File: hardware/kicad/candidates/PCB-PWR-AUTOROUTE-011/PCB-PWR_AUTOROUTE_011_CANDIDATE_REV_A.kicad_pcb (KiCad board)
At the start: 4 copper layers, 90 x 60 mm, 66 parts, among them J1 43045-0213, J2 43045-1202, Q1 CSD18540Q5B, U1 LM74700QDBVRQ1, U2 INA226AIDGSR, U3 LMR604403SRAKR, U4 LMR604403SRAKR, U5 TPS7A2018PDBVR

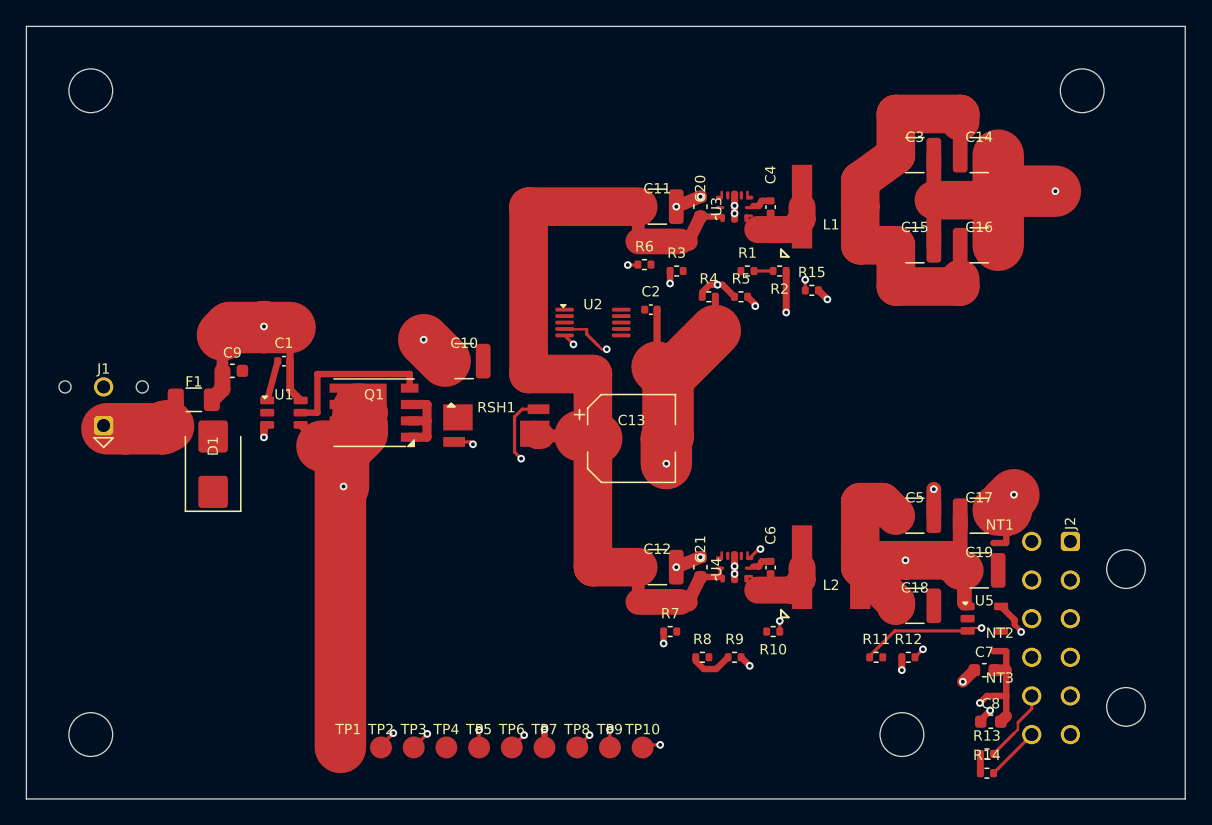
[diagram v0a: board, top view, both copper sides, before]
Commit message: apply: tools/apply_pcb_pwr_autoroute_candidate_rev_a.py
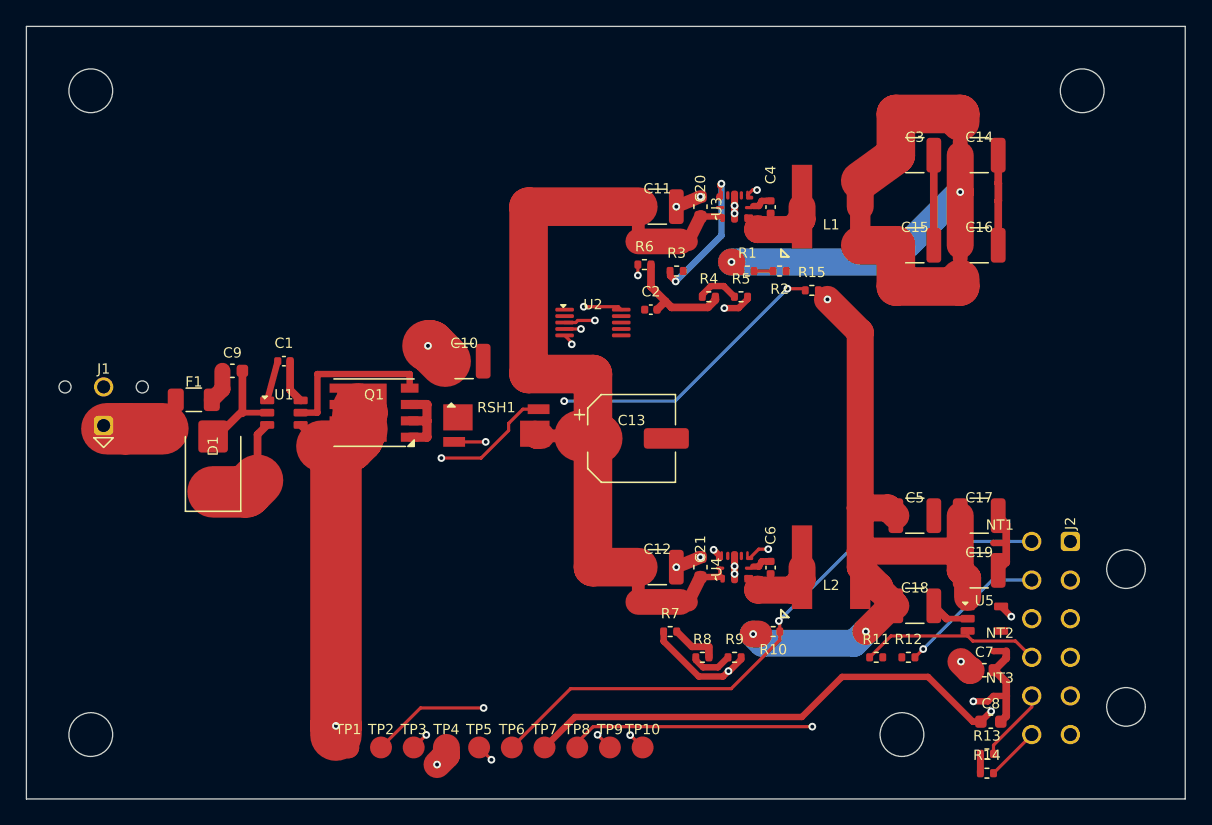
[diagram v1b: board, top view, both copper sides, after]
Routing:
- net 3V8_MODEM: track 34.0 -> 146.4 mm, vias 0 -> 3
- net FAULT: track 41.6 -> 82.8 mm, vias 2 -> 3
- net I2C2_SCL: track 73.4 -> 39.2 mm
- net I2C2_SDA: track 72.7 -> 40.0 mm
- net 3V3_DIGITAL: track 71.1 -> 93.9 mm
- net SHUNT_SOURCE_SENSE: track 28.0 -> 49.1 mm, vias 2 -> 3
- net VBAT_PROTECTED: track 53.5 -> 68.1 mm
- net EN_MODEM: track 50.4 -> 63.7 mm
- net VBAT_FUSED: track 33.2 -> 21.0 mm, vias 2 -> 0
- net GND_PWR: track 64.7 -> 53.3 mm, vias 13 -> 8
- net RT_3V3: track 9.28 -> 19.5 mm
- net RT_3V8: track 9.29 -> 18.3 mm, vias 2 -> 3
- net PG_3V8: track 55.8 -> 63.8 mm, vias 2 -> 4
- net 1V8_MIC: track 55.9 -> 52.9 mm, vias 3 -> 2
- net VBAT_RAW: track 7.51 -> 4.70 mm
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
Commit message: apply: tools/apply_pcb_pwr_autoroute_candidate_rev_a.py
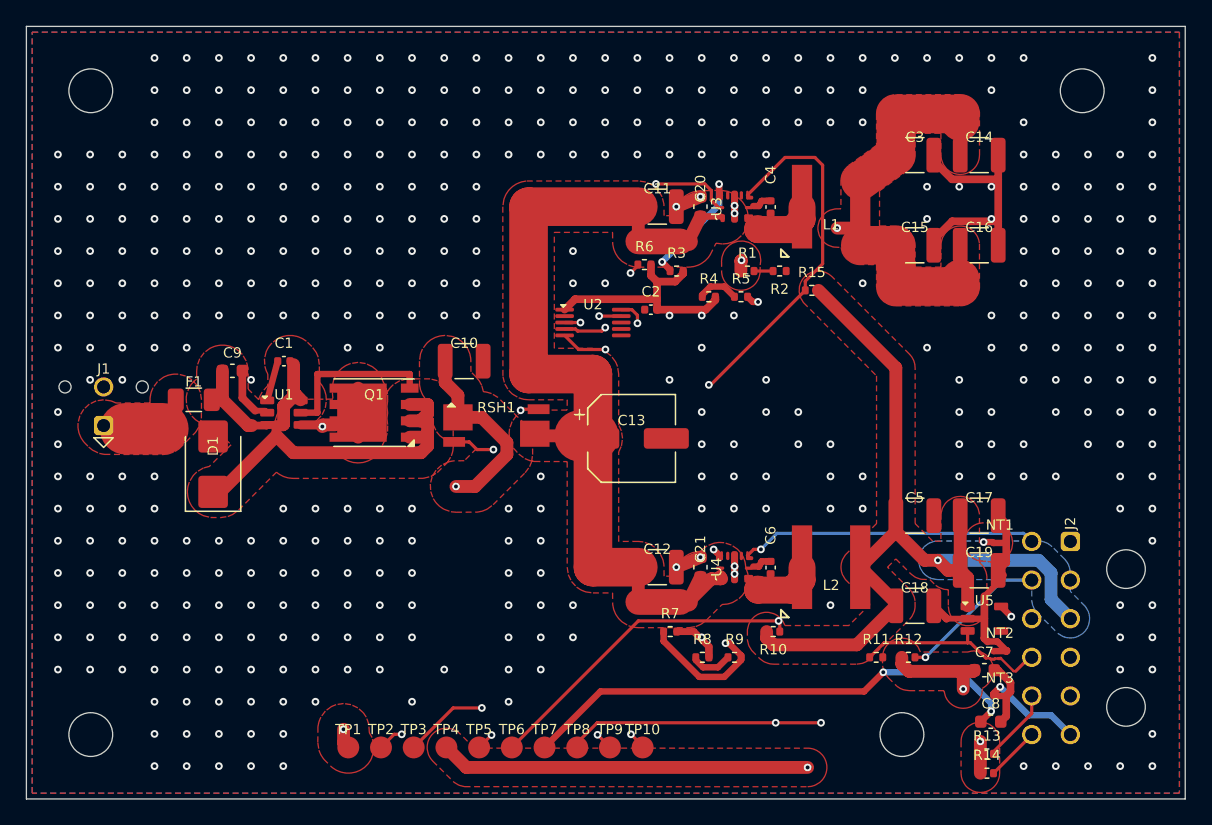
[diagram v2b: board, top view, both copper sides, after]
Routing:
- net VBAT_FUSED: track 21.0 -> 42.5 mm
- net GND_PWR: track 53.3 -> 72.7 mm, vias 8 -> 409
- net 3V8_MODEM: track 146.4 -> 132.3 mm
- net SHUNT_LOAD_SENSE: track 32.8 -> 43.9 mm, vias 2 -> 3
- net GND_MODEM: track 0.00 -> 8.74 mm, vias 0 -> 1
- net EN_MODEM: track 63.7 -> 71.9 mm, vias 1 -> 2
- net PG_3V8: track 63.8 -> 71.3 mm, vias 4 -> 2
- net VBAT_PROTECTED: track 68.1 -> 61.1 mm, vias 2 -> 3
- net I2C2_SDA: track 40.0 -> 45.3 mm
- net GND_MIC: track 11.7 -> 7.91 mm
- net 1V8_MIC: track 52.9 -> 55.7 mm, vias 2 -> 3
- net FAULT: track 82.8 -> 85.5 mm, vias 3 -> 4
- net VBAT_RAW: track 4.70 -> 7.37 mm
- net I2C2_SCL: track 39.2 -> 40.9 mm
- net SHUNT_SOURCE_SENSE: track 49.1 -> 50.7 mm
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- added copper zone on B.Cu, net 3V3_DIGITAL
- added copper zone on F.Cu, net 3V3_DIGITAL
- added copper zone on In2.Cu, net 3V3_DIGITAL
- added copper zone on F.Cu, net 3V8_MODEM
- added copper zone on In2.Cu, net 3V8_MODEM
- added copper zone on F.Cu, net GND_MODEM
- added copper zone on In2.Cu, net GND_MODEM
- added copper zone on B.Cu, net GND_PWR
- added copper zone on F.Cu, net GND_PWR
- added copper zone on F.Cu, net VBAT_FUSED
- added copper zone on F.Cu, net VBAT_PROTECTED
- added copper zone on In2.Cu, net VBAT_PROTECTED
- added copper zone on F.Cu, net VBAT_RAW
- added copper zone on F.Cu, net VBAT_SYS

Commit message: apply: tools/apply_pcb_pwr_autoroute_candidate_rev_a.py
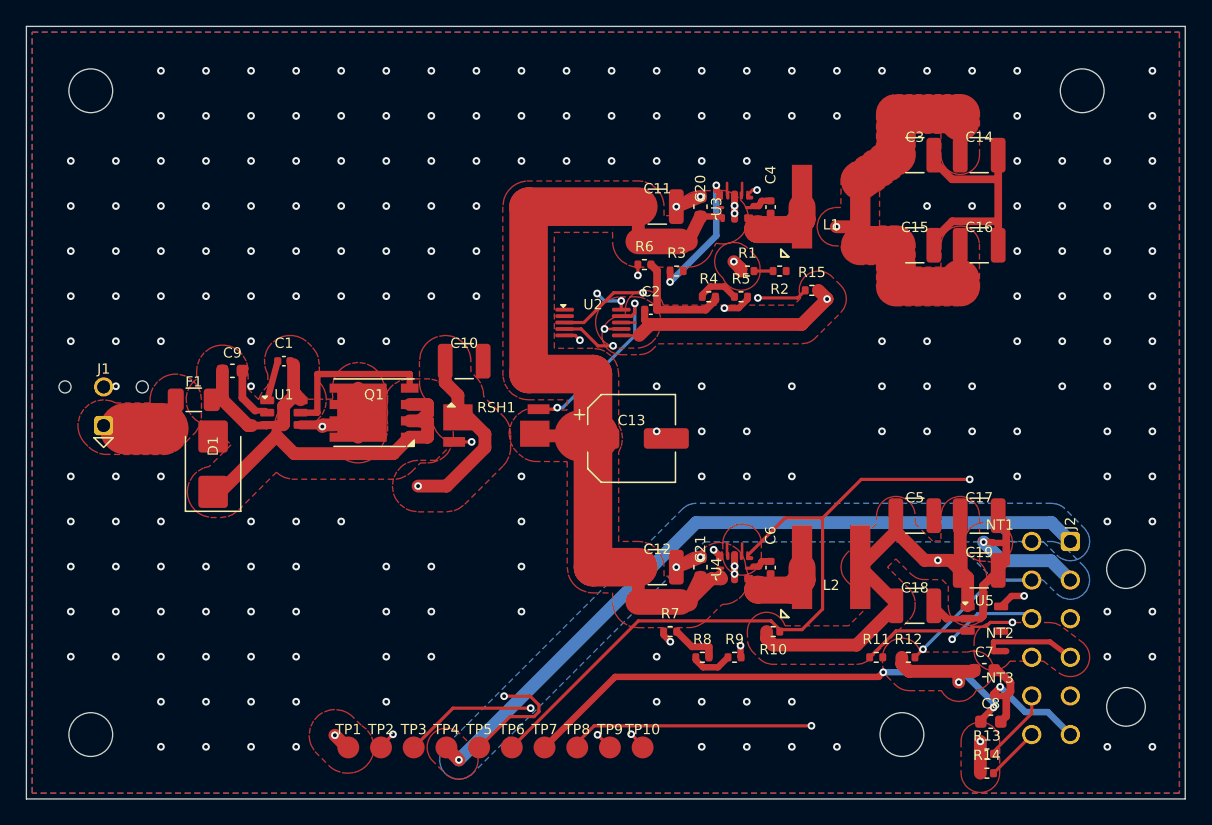
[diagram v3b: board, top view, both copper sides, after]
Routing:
- net EN_MODEM: track 71.9 -> 46.4 mm
- net 3V3_DIGITAL: track 93.9 -> 117.4 mm, vias 3 -> 4
- net GND_PWR: track 72.7 -> 59.8 mm, vias 409 -> 213
- net PWR_GOOD: track 55.1 -> 63.2 mm, vias 2 -> 1
- net GND_DIGITAL: track 0.00 -> 7.10 mm
- net SHUNT_LOAD_SENSE: track 43.9 -> 48.8 mm
- net I2C2_SDA: track 45.3 -> 40.7 mm
- net VBAT_PROTECTED: track 61.1 -> 56.7 mm
- net SHUNT_SOURCE_SENSE: track 50.7 -> 46.4 mm, vias 3 -> 4
- net RT_3V3: track 19.1 -> 15.7 mm, vias 2 -> 3
- net 3V8_MODEM: track 132.3 -> 134.9 mm
- net VBAT_FUSED: track 42.5 -> 40.7 mm
- net PG_3V8: track 71.3 -> 69.7 mm, vias 2 -> 3
- net 1V8_MIC: track 55.7 -> 57.2 mm
- net RT_3V8: track 19.8 -> 18.5 mm
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- added copper zone on B.Cu, net 3V8_MODEM
- added copper zone on F.Cu, net GND_DIGITAL
- added copper zone on B.Cu, net GND_MODEM
- removed copper zone on B.Cu, net 3V3_DIGITAL
- removed copper zone on In2.Cu, net GND_MODEM

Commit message: apply: tools/apply_pcb_pwr_autoroute_candidate_rev_a.py
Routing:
- net I2C2_SCL: track 39.7 -> 76.5 mm
- net RT_3V8: track 18.5 -> 0.35 mm, vias 3 -> 0
- net PG_3V8: track 69.7 -> 53.0 mm, vias 3 -> 2
- net 3V3_DIGITAL: track 117.4 -> 103.0 mm, vias 4 -> 5
- net EN_MODEM: track 46.4 -> 58.0 mm
- net EN_AUX: track 15.5 -> 24.5 mm, vias 1 -> 0
- net RT_3V3: track 15.7 -> 9.45 mm, vias 3 -> 0
- net GND_PWR: track 59.8 -> 65.3 mm
- net VBAT_PROTECTED: track 56.7 -> 60.0 mm
- net 1V8_MIC: track 57.2 -> 59.7 mm
- net SHUNT_LOAD_SENSE: track 48.8 -> 46.6 mm
- net FAULT: track 85.0 -> 83.4 mm
- net 3V8_MODEM: track 134.9 -> 135.6 mm
- net SHUNT_SOURCE_SENSE: track 46.4 -> 46.7 mm, vias 4 -> 3
- net MODE_3V3: track 4.24 -> 4.49 mm, vias 0 -> 1
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
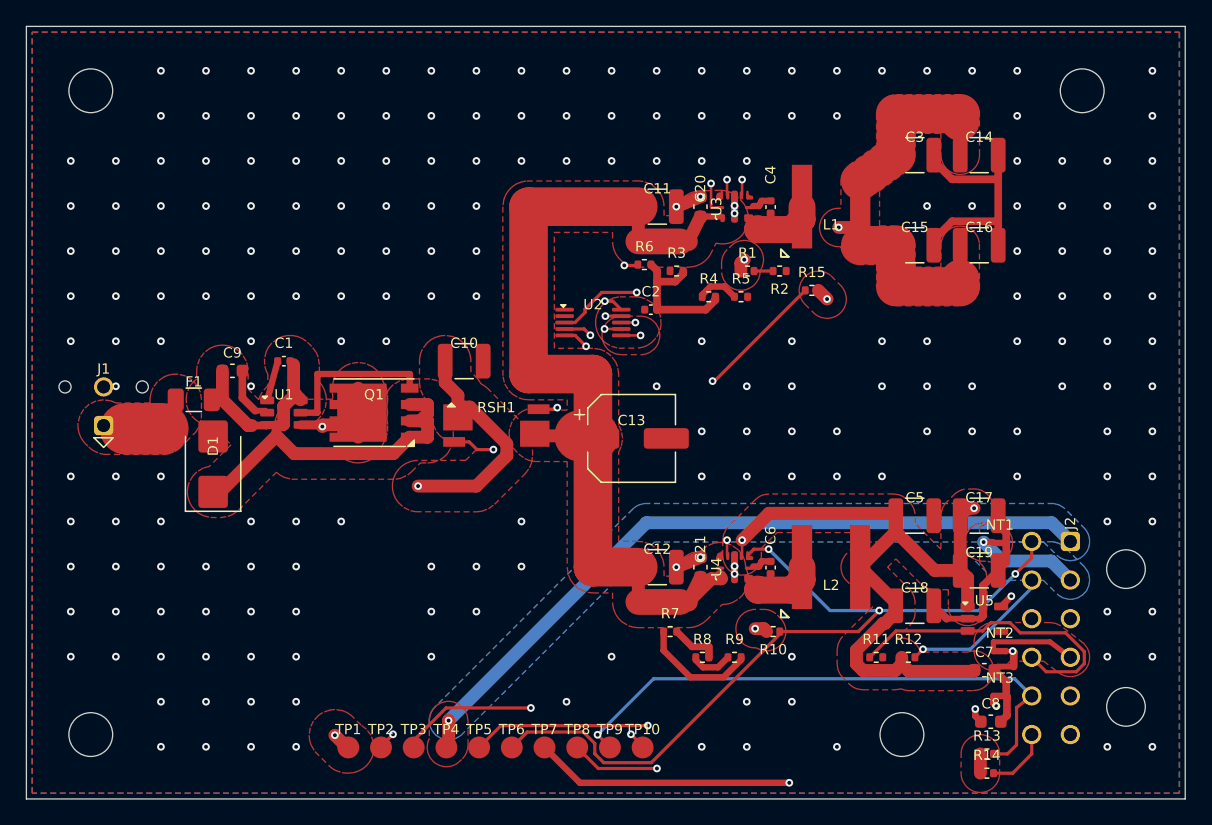
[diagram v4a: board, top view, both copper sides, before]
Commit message: apply: tools/apply_pcb_pwr_autoroute_candidate_rev_a.py
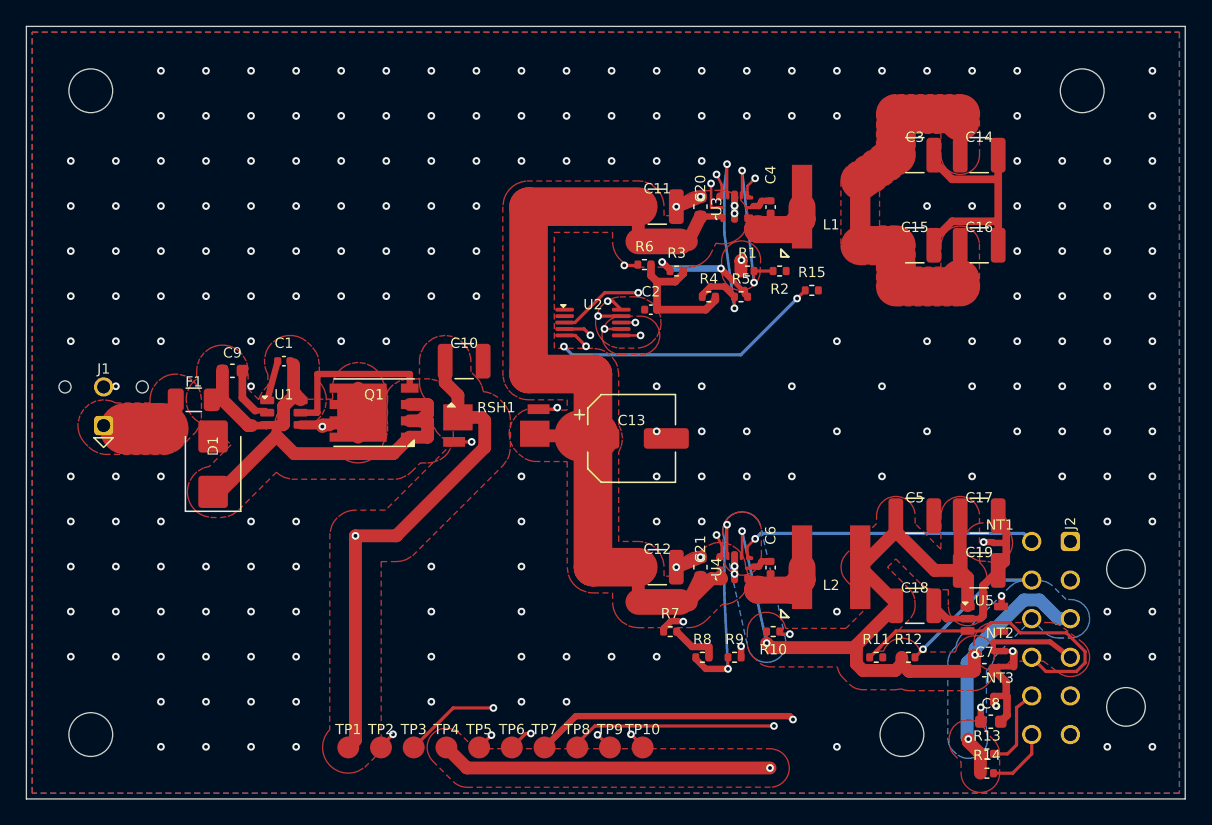
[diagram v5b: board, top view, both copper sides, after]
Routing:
- net I2C2_SCL: track 76.5 -> 40.4 mm
- net 3V3_DIGITAL: track 103.0 -> 80.5 mm
- net RT_3V8: track 0.35 -> 18.4 mm, vias 0 -> 3
- net PG_3V8: track 53.0 -> 67.8 mm, vias 2 -> 4
- net MODE_3V8: track 4.47 -> 17.8 mm, vias 1 -> 2
- net MODE_3V3: track 4.49 -> 17.5 mm, vias 1 -> 2
- net FB_3V8: track 2.71 -> 13.1 mm, vias 1 -> 2
- net RT_3V3: track 9.45 -> 17.2 mm, vias 0 -> 3
- net 3V8_MODEM: track 135.6 -> 142.7 mm, vias 3 -> 2
- net PWR_GOOD: track 63.0 -> 59.0 mm
- net VBAT_PROTECTED: track 60.0 -> 57.6 mm, vias 3 -> 2
- net SHUNT_LOAD_SENSE: track 46.6 -> 44.6 mm
- net 1V8_MIC: track 59.7 -> 57.7 mm
- net FAULT: track 83.4 -> 85.3 mm
- net SHUNT_SOURCE_SENSE: track 46.7 -> 45.1 mm
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- added copper zone on B.Cu, net 3V3_DIGITAL
- added copper zone on In2.Cu, net GND_MODEM
- removed copper zone on In2.Cu, net 3V3_DIGITAL
- removed copper zone on B.Cu, net 3V8_MODEM
- removed copper zone on B.Cu, net GND_MODEM

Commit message: apply: tools/apply_pcb_pwr_autoroute_candidate_rev_a.py
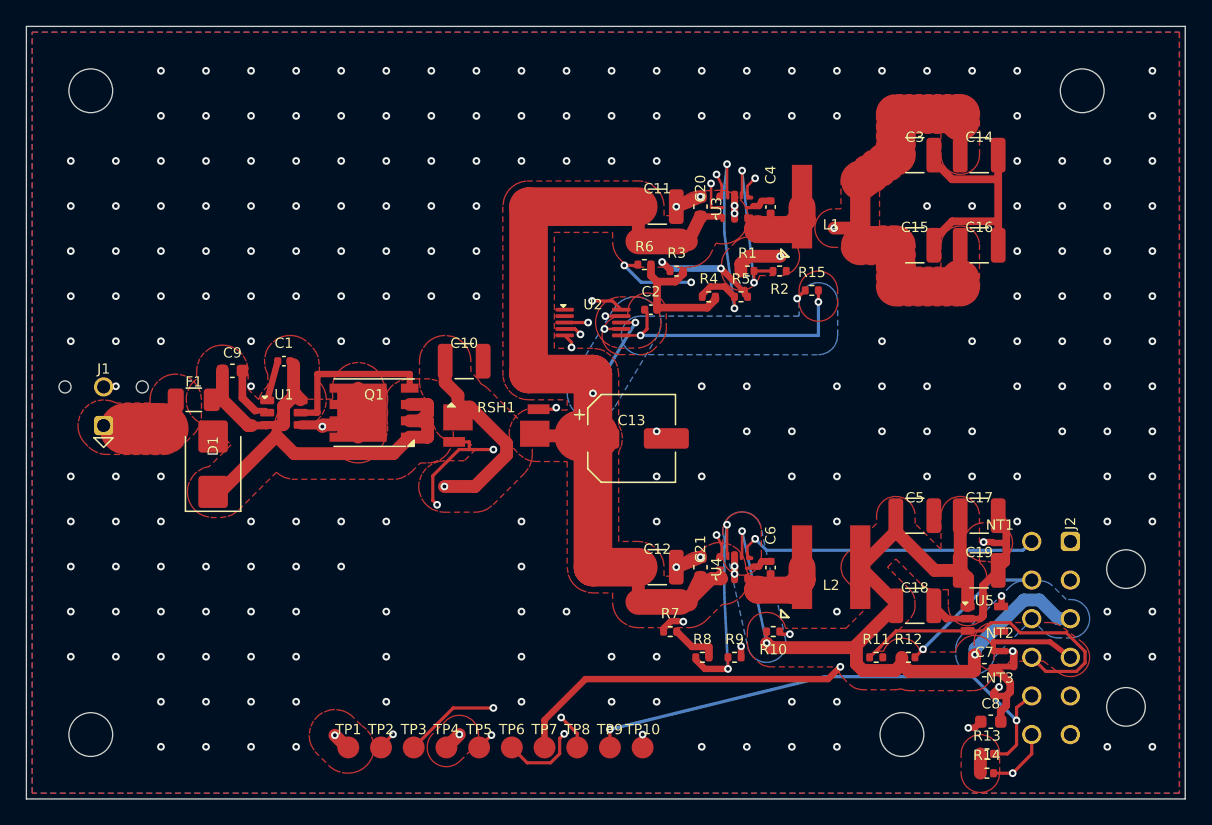
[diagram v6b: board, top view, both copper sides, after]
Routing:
- net I2C2_SDA: track 41.0 -> 83.1 mm, vias 2 -> 3
- net I2C2_SCL: track 40.4 -> 78.2 mm, vias 2 -> 3
- net 1V8_MIC: track 57.7 -> 70.4 mm
- net 3V3_DIGITAL: track 80.5 -> 91.4 mm
- net FAULT: track 85.3 -> 77.0 mm
- net VBAT_SYS: track 76.2 -> 82.6 mm, vias 1 -> 2
- net PWR_GOOD: track 59.0 -> 65.0 mm
- net SHUNT_SOURCE_SENSE: track 45.1 -> 47.8 mm, vias 3 -> 4
- net VBAT_PROTECTED: track 57.6 -> 60.1 mm, vias 2 -> 3
- net 3V8_MODEM: track 142.7 -> 144.0 mm, vias 2 -> 3
- net EN_MODEM: track 58.0 -> 57.1 mm, vias 2 -> 3
- net PG_3V8: track 67.8 -> 67.0 mm, vias 4 -> 3
- net SHUNT_LOAD_SENSE: track 44.6 -> 45.3 mm
- net GND_PWR: track 65.3 -> 65.5 mm, vias 214 -> 220
- added copper zone on B.Cu, net VBAT_SYS
